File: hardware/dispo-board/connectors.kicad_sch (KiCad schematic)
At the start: 23 parts, among them J1 USB_B_Micro, J10 Conn_01x02, J11 Conn_01x02, J12 Conn_01x03, J13 Conn_01x03, J2 Conn_01x03, J3 Conn_01x03, J4 Conn_01x03, J5 Conn_01x02, J6 Conn_01x02, J7 Conn_01x02, J8 Conn_01x02, J9 Conn_01x04

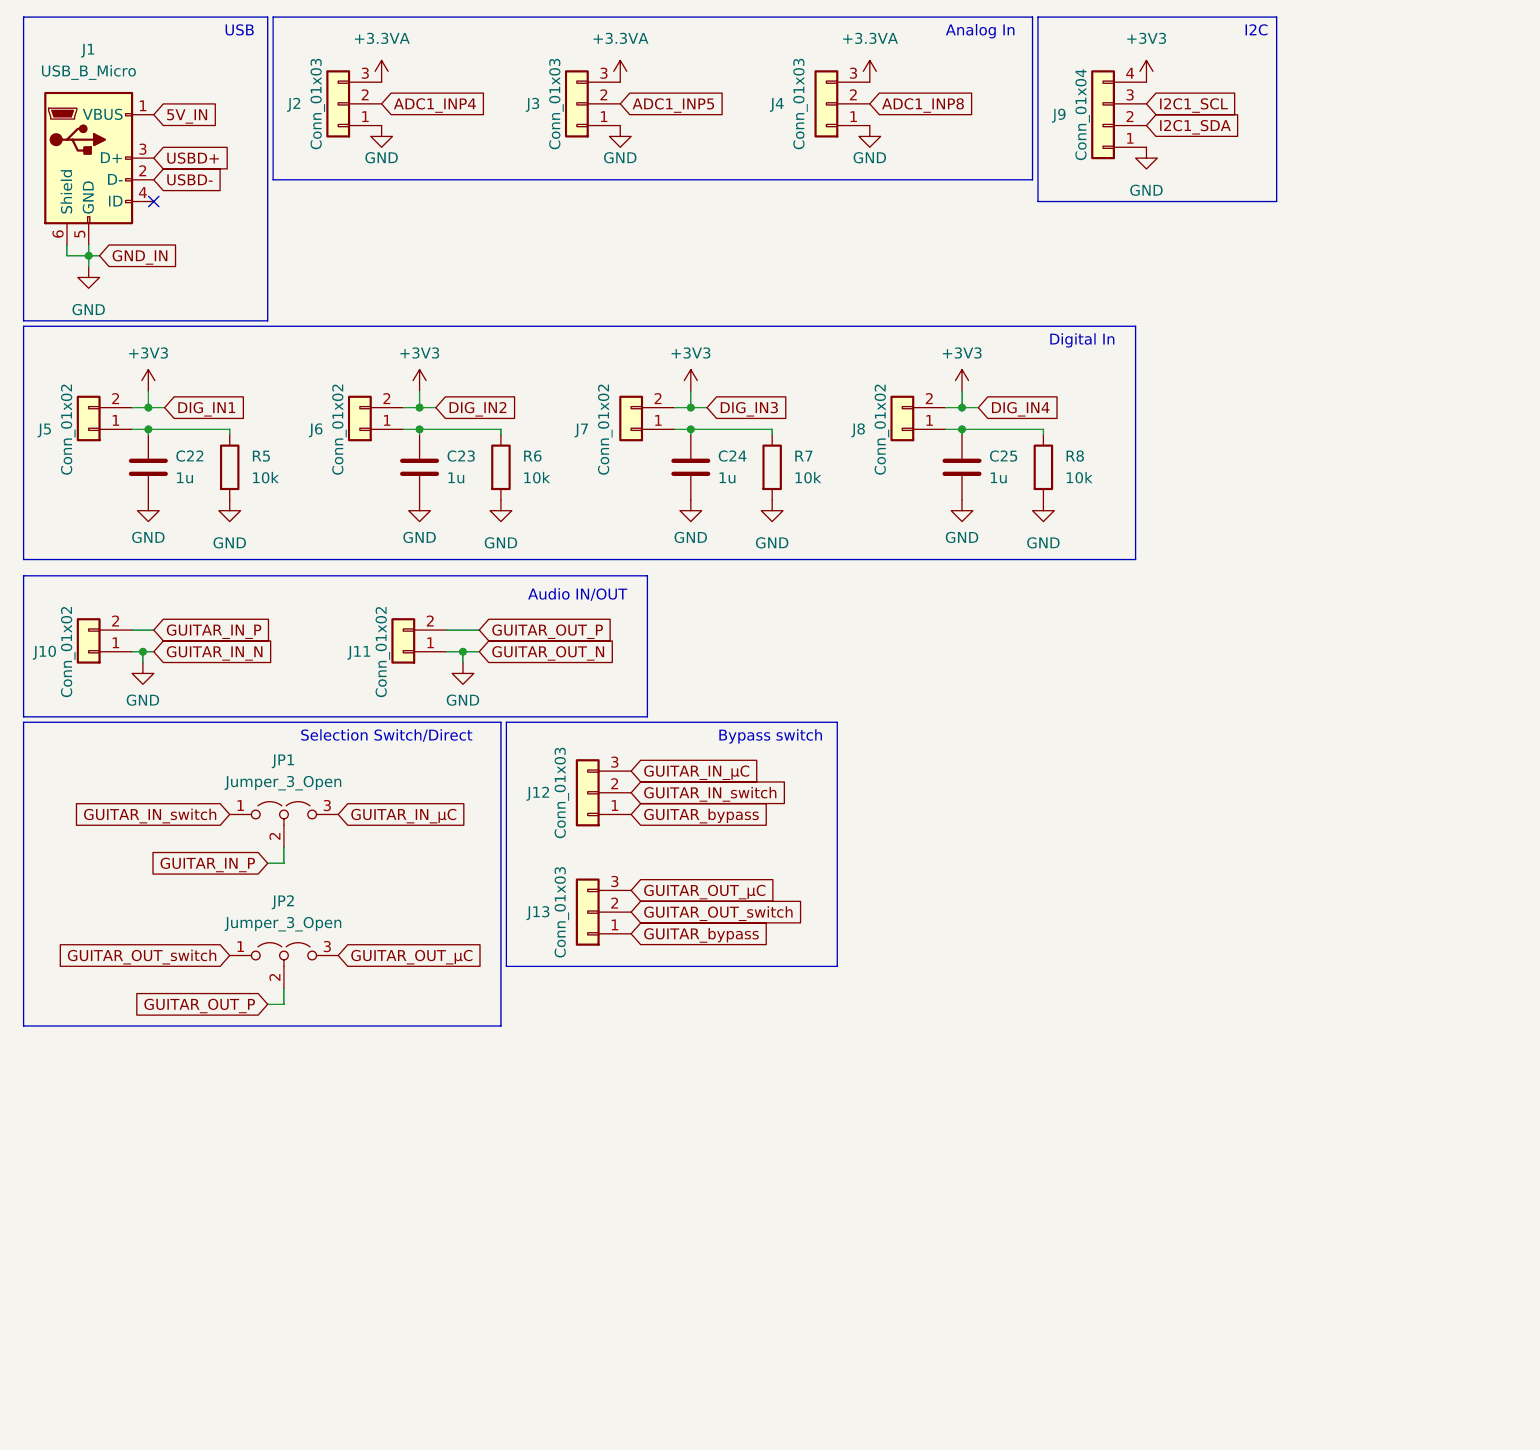
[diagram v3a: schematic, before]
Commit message: added debugger, corrected erc errors
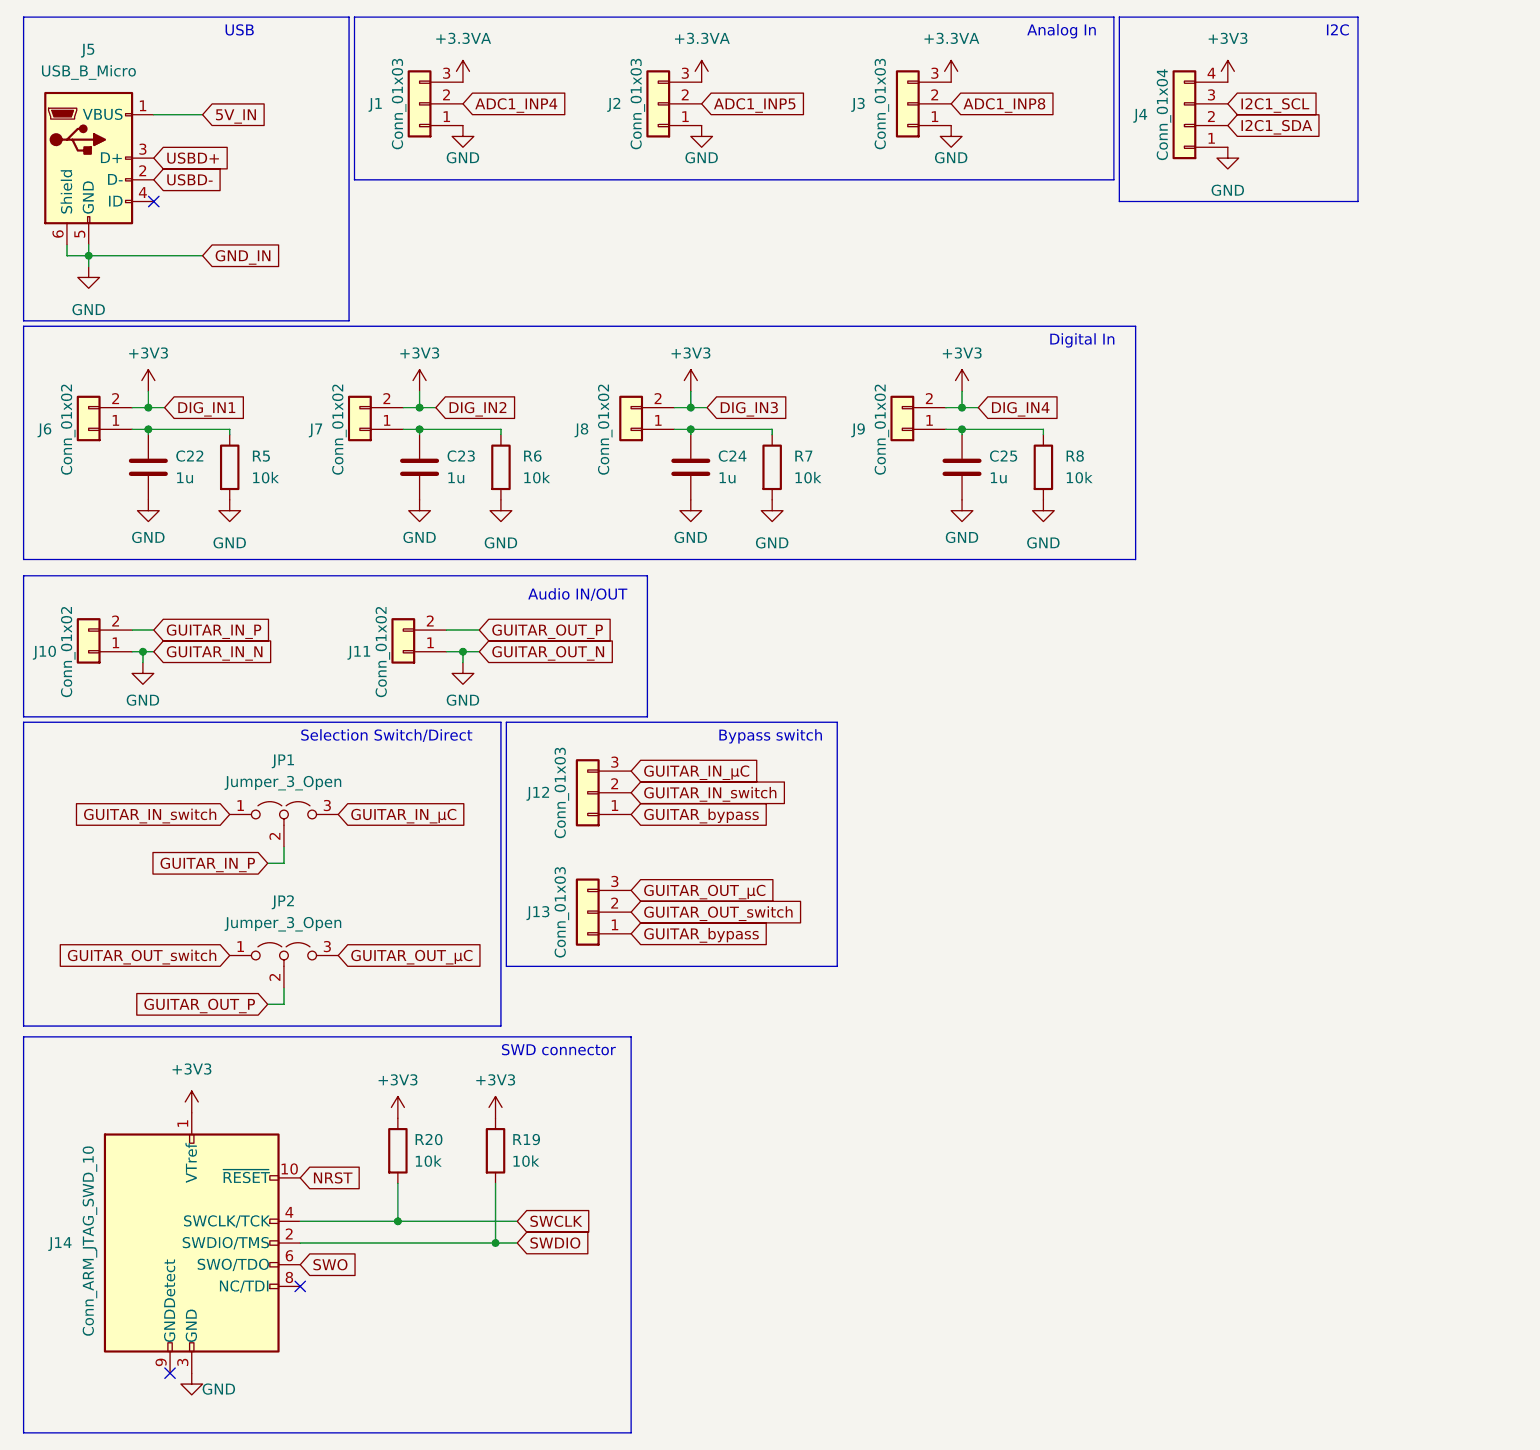
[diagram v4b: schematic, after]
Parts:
- added J14: Conn_ARM_JTAG_SWD_10, Connector_PinHeader_1.27mm:PinHeader_2x05_P1.27mm_Vertical, symbol Connector:Conn_ARM_JTAG_SWD_10
- added R19, R20: 10k, symbol Device:R
- renumbered J2 to J1, J3 to J2, J4 to J3, J9 to J4, J1 to J5, J5 to J6, J6 to J7, J7 to J8, J8 to J9
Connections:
- net +3V3: now also J14.1 (VTref), R19.1, R20.1
- net GND: now also J14.3 (GND), J14.5 (GND)
- new net NRST: J14.10 (~{RESET})
- new net SWCLK: J14.4 (SWCLK/TCK), R20.2
- new net SWDIO: J14.2 (SWDIO/TMS), R19.2
- new net SWO: J14.6 (SWO/TDO)
- no-connect marks 1 -> 3
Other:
- note added: "SWD connector"
- moved on the sheet: J1, J2, J3, J4

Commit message: added footprints and mouser nrs
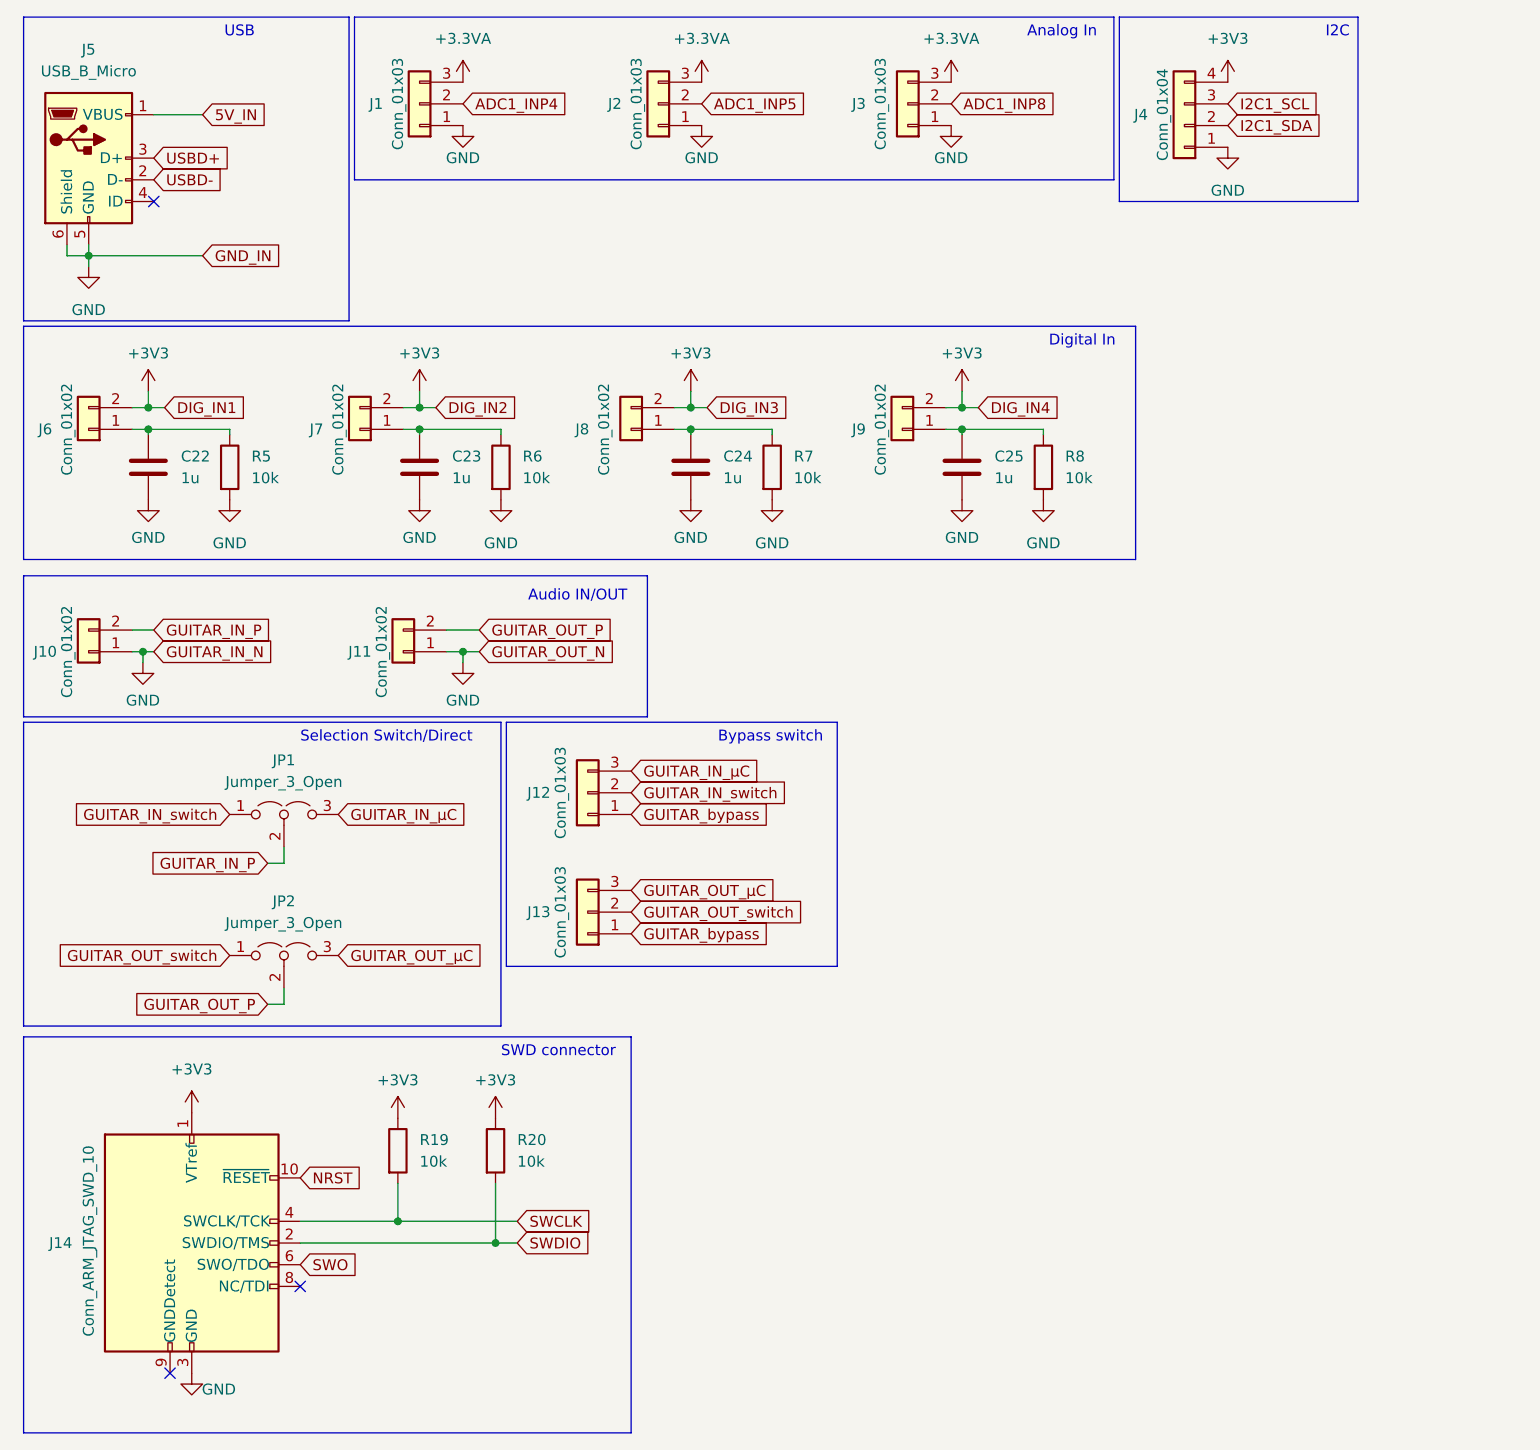
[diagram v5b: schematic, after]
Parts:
- C22, C23, C24, C25: footprint (none) -> Capacitor_SMD:C_0603_1608Metric; MOUSER_NR (none) -> 81-GRM185R61C105KE4J
- J14: MOUSER_NR (none) -> 474-PRT-15362
- R19, R20, R5, R6, R7, R8: footprint (none) -> Resistor_SMD:R_0402_1005Metric; MOUSER_NR (none) -> 71-CRCW040210K0FKEDC
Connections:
- net SWCLK: now also R19.2; no longer R20.2
- net SWDIO: now also R20.2; no longer R19.2

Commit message: few changes supply op amp, anaolg input and output, updated footprints and mouser nrs
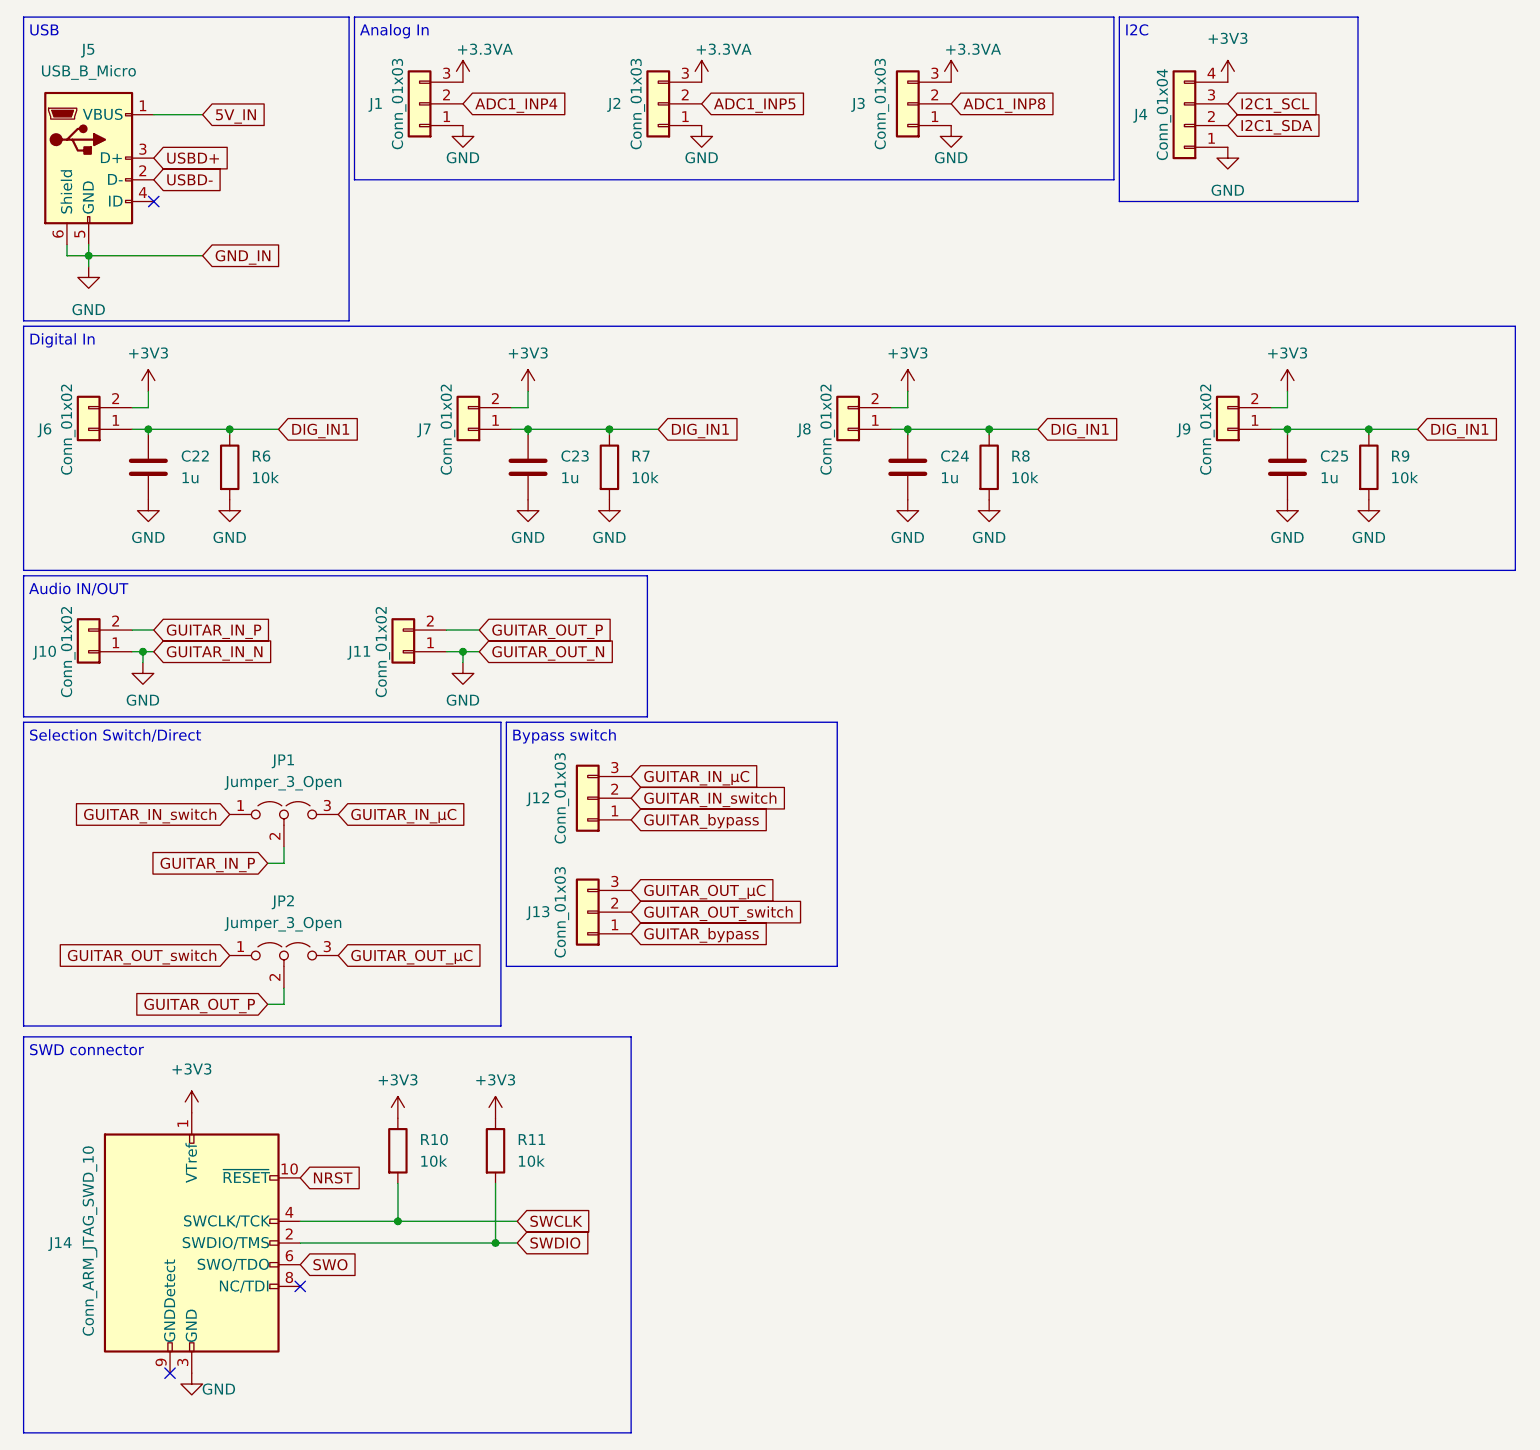
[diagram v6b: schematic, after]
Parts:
- removed R6: 10k, Resistor_SMD:R_0402_1005Metric, symbol Device:R
- added R9: 10k, Resistor_SMD:R_0402_1005Metric, symbol Device:R
- renumbered R19 to R10, R20 to R11, R5 to R6
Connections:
- net GND: now also R9.2
- net DIG_IN1: now reaches C22.1, J6.1 (Pin_1), R6.1
- net DIG_IN1: now also C23.1, C24.1, C25.1, J7.1 (Pin_1), J8.1 (Pin_1), J9.1 (Pin_1), R7.1, R8.1, R9.1
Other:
- moved on the sheet: J12

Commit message: added missing footprint
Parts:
- JP1, JP2: footprint (none) -> Connector_PinHeader_2.54mm:PinHeader_1x03_P2.54mm_Vertical
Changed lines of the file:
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@@
       (effects (font (size 1.27 1.27)))
     )
-    (property "Footprint" "" (at 49.53 111.76 0)
+    (property "Footprint" "Connector_PinHeader_2.54mm:PinHeader_1x03_P2.54mm_Vertical" (at 49.53 111.76 0)
       (effects (font (size 1.27 1.27)) hide)
     )
@@
       (effects (font (size 1.27 1.27)))
     )
-    (property "Footprint" "" (at 49.53 128.27 0)
+    (property "Footprint" "Connector_PinHeader_2.54mm:PinHeader_1x03_P2.54mm_Vertical" (at 49.53 128.27 0)
       (effects (font (size 1.27 1.27)) hide)
     )
